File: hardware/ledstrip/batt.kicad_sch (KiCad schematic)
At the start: 51 parts, among them J4 BMS connectors, Q10 Q_PMOS, Q5 Q_NMOS, Q6 Q_NMOS, Q7 Q_NMOS, Q8 Q_NMOS, U5 BQ25703A, U7 TL431DBZ

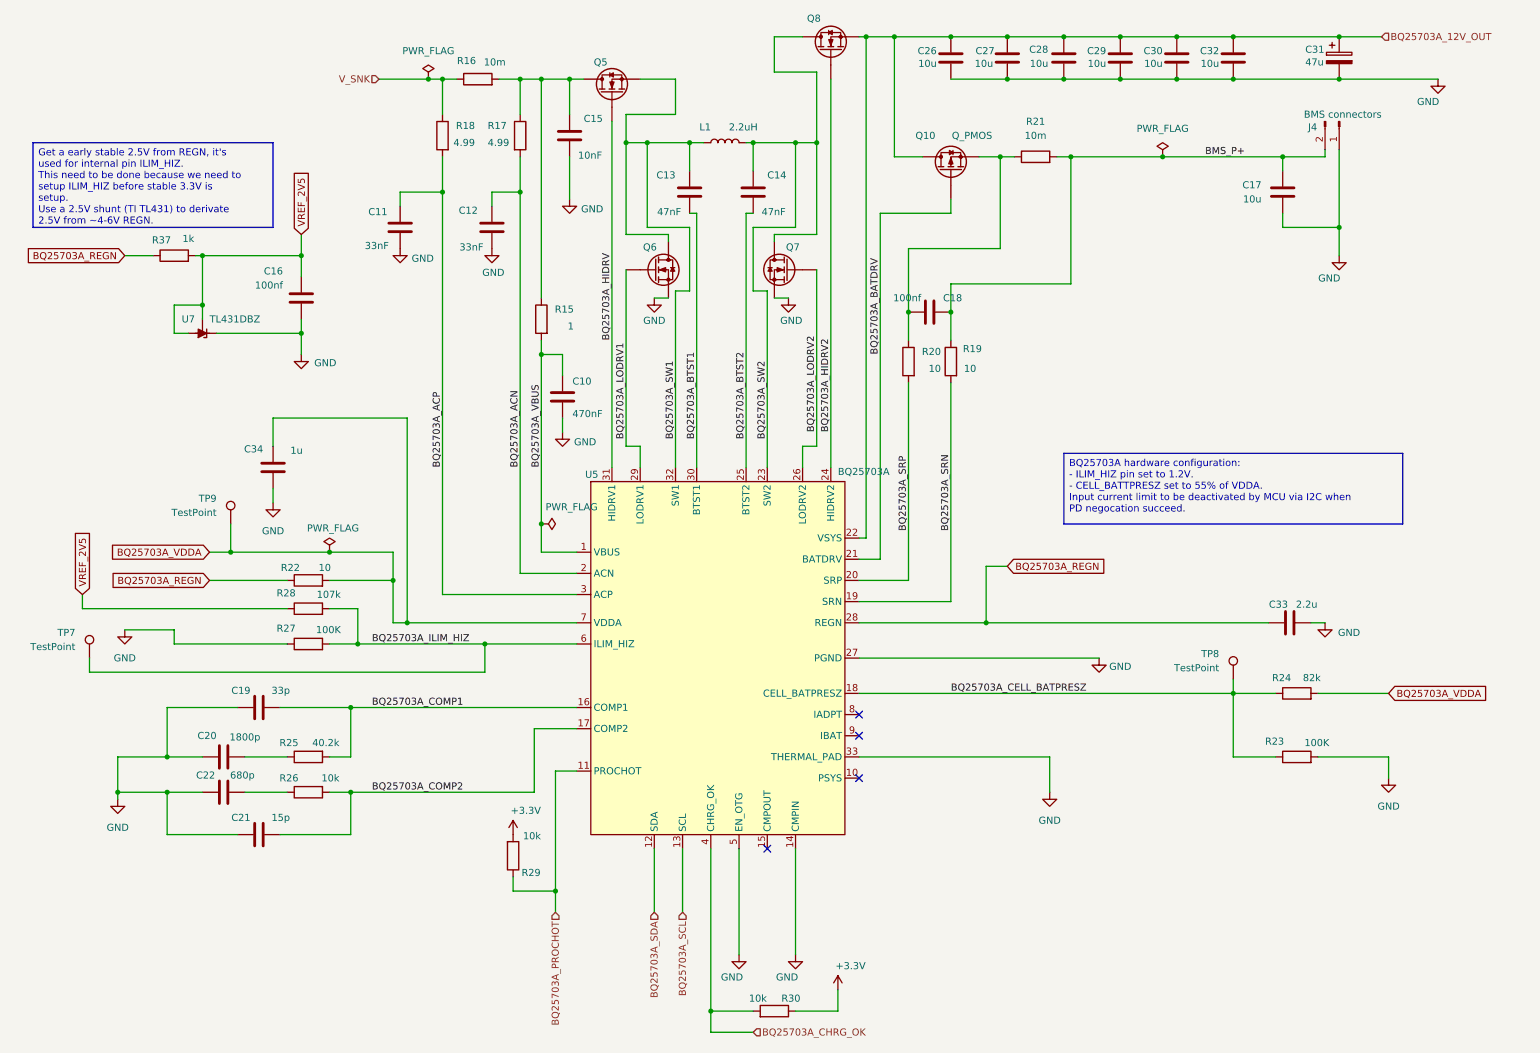
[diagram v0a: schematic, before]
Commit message: Add a lot of TestPoints
Move P-FET at the edge of board.
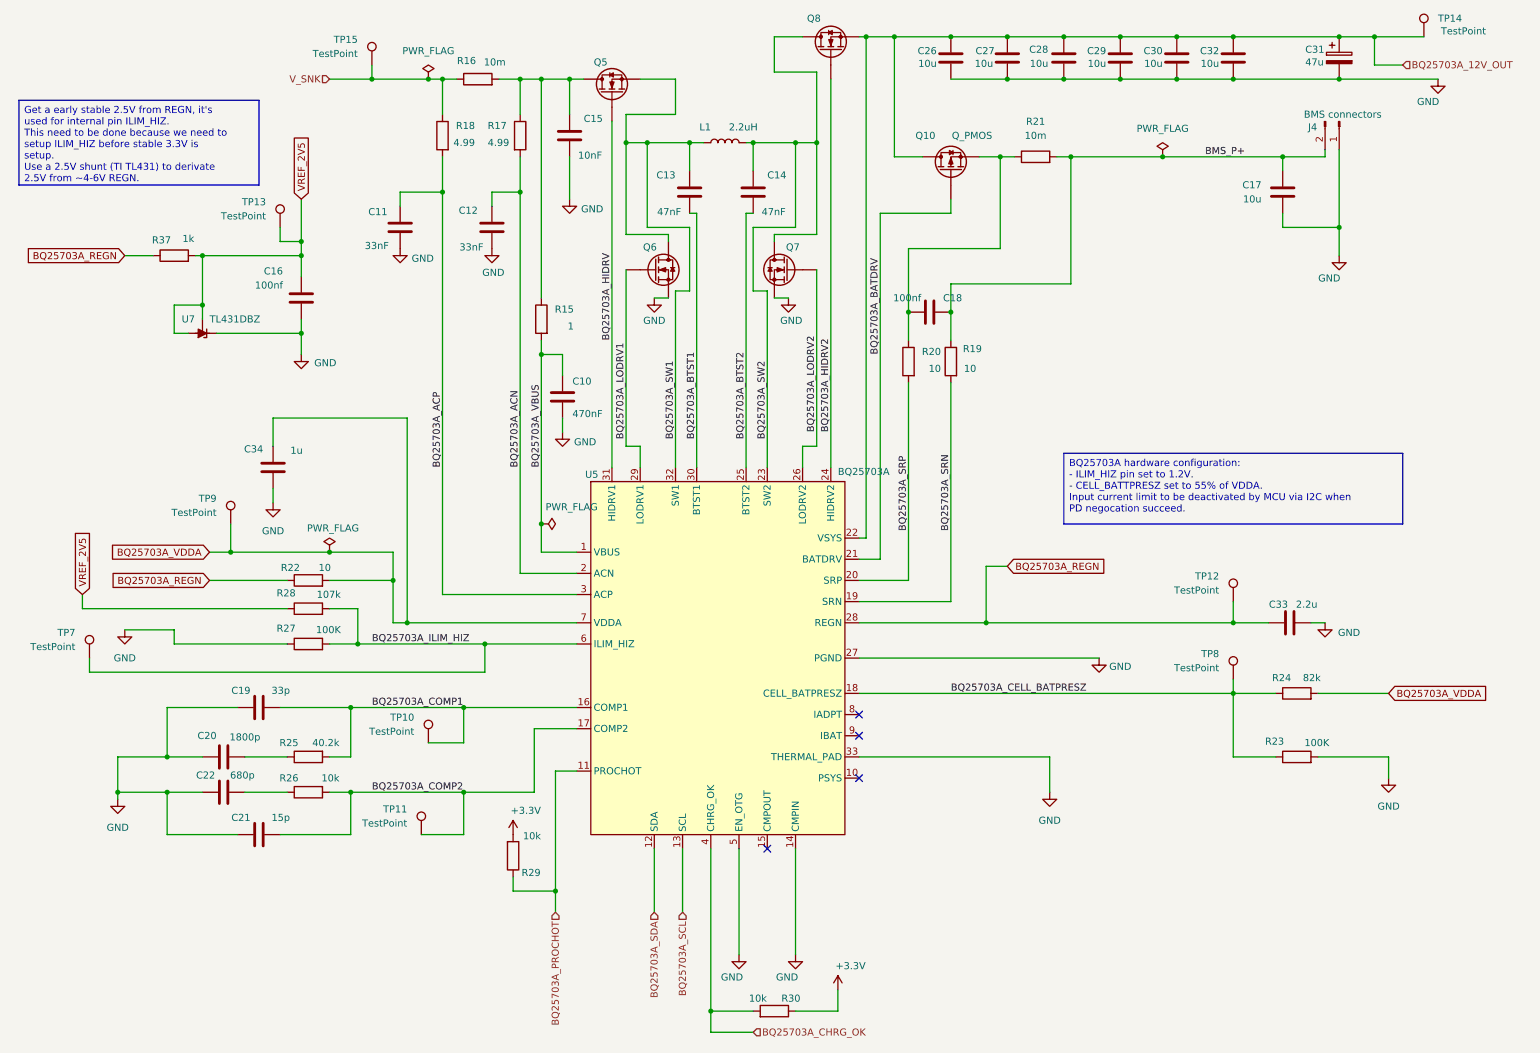
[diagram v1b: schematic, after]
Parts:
- added TP10, TP11, TP12, TP13, TP14, TP15: TestPoint, TestPoint:TestPoint_Pad_1.0x1.0mm, symbol Connector:TestPoint
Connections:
- net BQ25703A_12V_OUT: now also TP14.1
- net BQ25703A_COMP1: now also TP10.1
- net BQ25703A_COMP2: now also TP11.1
- net BQ25703A_REGN: now also TP12.1
- net VREF_2V5: now also TP13.1
- net V_SNK: now also TP15.1

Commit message: Add distributor link for battery pack.
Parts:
- J4: Distributor Link 1 (none) -> https://www.amazon.fr/-/en/Replacement-Battery-Lansing-INR1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
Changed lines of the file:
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@@
 		(exclude_from_sim no)
 		(in_bom yes)
-		(on_board yes)
+		(on_board no)
 		(dnp no)
 		(property "Reference" "J4"
@@
 			(effects
 				(font
+					(size 1.27 1.27)
+				)
+				(hide yes)
+			)
+		)
+		(property "Distributor Link 1" "https://www.amazon.fr/-/en/Replacement-Battery-Lansing-INR18650-3S-Speaker/dp/B092W4FK3K?dib=eyJ2IjoiMSJ9.4PBGI1Q5coJoF5Wz5QmfktwUjoLxbsDeJVbRkYsUVfosZjpfj8Rx4OzMnoGtUwiyFIFBs5UOxeYU4lRFbgH33roWmlGkPoeXzYvMblbZEgzJ9n-oVUj-gsPHuzrdELBOigTMx7sczVBMmwx9dP5PWb4c_t_3eSytQFVCVcDTZrvwMcUFK2y6TdJNQU6zrjeWByuhpRnuXuwWIMSWdTXQIqcjxK-vLdTeK6InaDQqMCxeQIEnfFnwOO9I2DD-PfEIaYszstYRr76Wom0X5zB9SxwDJJopwYIkp9XlafZ1Edo.iLT02tmwuz1moqDpkQanjm0GHqT79PlbLw9HF6uW4KA&dib_tag=se&keywords=batterie+3s+11.1v+bms&qid=1773512814&sr=8-30"
+			(at 252.73 31.75 90)
+			(effects
+				(font

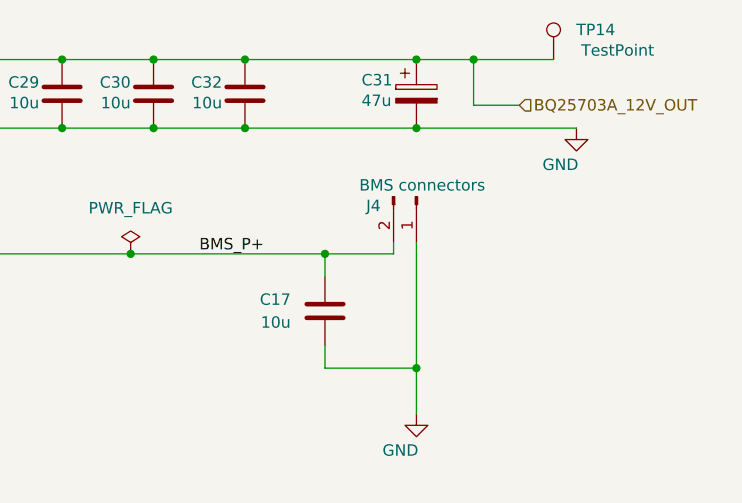
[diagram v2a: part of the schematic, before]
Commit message: Improve BOM: exclude uneeded parts, add some columns.
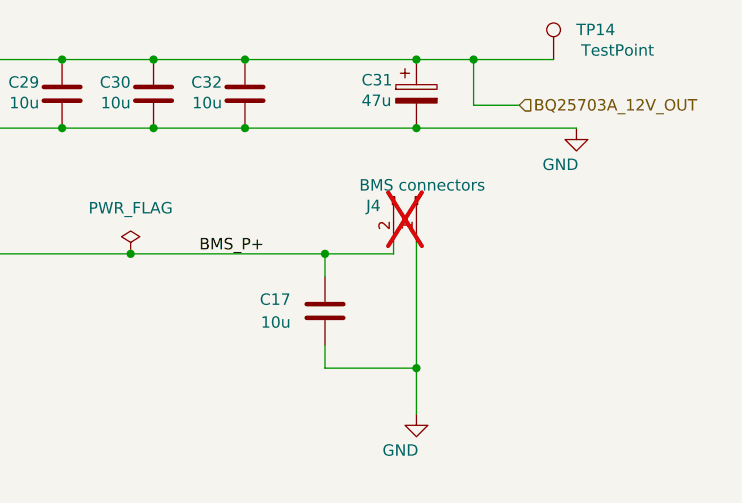
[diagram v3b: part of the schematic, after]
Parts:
- J4: now not fitted
- TP10, TP11, TP12, TP13, TP14, TP15, TP7, TP8, TP9: now left out of the parts list

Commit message: Fix wrong footprint (C_0603 instead of R_0603)
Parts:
- R37: footprint Capacitor_SMD:C_0603_1608Metric -> Resistor_SMD:R_0603_1608Metric
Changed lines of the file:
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@@
 			)
 		)
-		(property "Footprint" "Capacitor_SMD:C_0603_1608Metric"
+		(property "Footprint" "Resistor_SMD:R_0603_1608Metric"
 			(at 43.18 57.658 90)
 			(effects
